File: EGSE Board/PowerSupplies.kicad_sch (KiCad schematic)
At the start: 30 parts, among them U1 VOR2121A8, U2 VOR2121A8, U3 INA238AQDGSRQ1, U4 INA238AQDGSRQ1, U5 INA238AQDGSRQ1, U7 ISO1540, U9 LD1117S33TR_SOT223

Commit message: Change to heater power
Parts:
- removed C10: 100nF, symbol Device:C_Small
- removed C7, C9: 10nF, symbol Device:C_Small
- removed U3, U5: INA238AQDGSRQ1, Package_SO:VSSOP-10_3x3mm_P0.5mm, symbol Power_Management:INA238AQDGSRQ1
- added C3, C5: 100nF, symbol Device:C_Small
- added R1: 0.1R, symbol Device:R
- added U14: INA3221, Package_DFN_QFN:Texas_RGV_S-PVQFN-N16_EP2.1x2.1mm, symbol Power_Management:INA3221
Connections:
- net +3V3: now also C5.1, U14.4 (VS)
- net DETEC_+12VA: now also U14.11 (IN-1)
- net DETEC_+3v3: now also U14.14 (IN-2)
- net GND: now also C3.2, C5.2, U14.3 (GND)
- net SCL: now also U14.6 (SCL)
- net SDA: now also U14.7 (SDA)
- net at R1.1, U1.7 (S1'): now also U14.12 (IN+1)
- net at R5.1, U2.8 (S1): now also U14.15 (IN+2)
- new net: R1.1, U14.2 (IN+3)
- new net DETEC_HTR: C3.1, R1.2, U14.1 (IN-3)
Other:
- note added: "I2C current monitors for +12 and +3v3 and heater supplies"
- note removed: "I2C current monitors for +12 and +3v3 supplies"
- moved on the sheet: C5, C6, R1, R5

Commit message: Friday updates. PCB first draft
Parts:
- C1, C2, C6: footprint (none) -> Capacitor_Tantalum_SMD:CP_EIA-7343-31_Kemet-D_Pad2.25x2.55mm_HandSolder
- C10, C3, C4, C5, C8: footprint (none) -> Capacitor_SMD:C_0402_1005Metric
- R1, R5: footprint (none) -> Resistor_THT:R_Axial_DIN0207_L6.3mm_D2.5mm_P7.62mm_Horizontal
- R1, R2: value 1R -> 0.1R; footprint (none) -> Resistor_THT:R_Axial_DIN0207_L6.3mm_D2.5mm_P7.62mm_Horizontal
- R13, R14, R3, R4, R6: footprint (none) -> Resistor_SMD:R_0612_1632Metric
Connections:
- net +3V3: now also U1.6 (S2); no longer U2.7 (S1')
- net -12V_Unswitched: now also U2.6 (S2); no longer U1.5 (S2'), U4.2 (A0)
- net DETEC_+12VA: now also U14.1 (IN-3); no longer U14.11 (IN-1)
- net DETEC_+3v3: now also U14.11 (IN-1); no longer U14.14 (IN-2)
- net DETEC_HTR: now also U14.14 (IN-2); no longer U14.1 (IN-3)
- net GND: now also U14.5 (A0), U2.4; no longer U2.2
- net at C10.2, C3.1, R13.1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: now also U4.2 (A0)
- net at C8.1, R2.1, U4.10 (IN+): now also U2.5 (S2'); no longer U1.6 (S2)
- net at R6.2: now also U1.3; no longer U2.1
- net at U14.2 (IN+3): now also R1.1, U1.7 (S1'); no longer R1.1
- net at U2.3: now also R4.2
- net +12_Unswitched: no longer names the net of C5.1, PS1.6 (+Vout), U1.8 (S1)
- new net: R5.1, U1.5 (S2'), U14.12 (IN+1)
- new net +12V_HTR: R1.1, U14.15 (IN+2)
- now unconnected: U2.8 (S1)
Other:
- note added: "A0,A1=Vs, address=0x45"
- note added: "A0=GND Address=0x40"
- moved on the sheet: C3, C5, C6, R1, R3, R4, R5, R6, U1, U14, U2

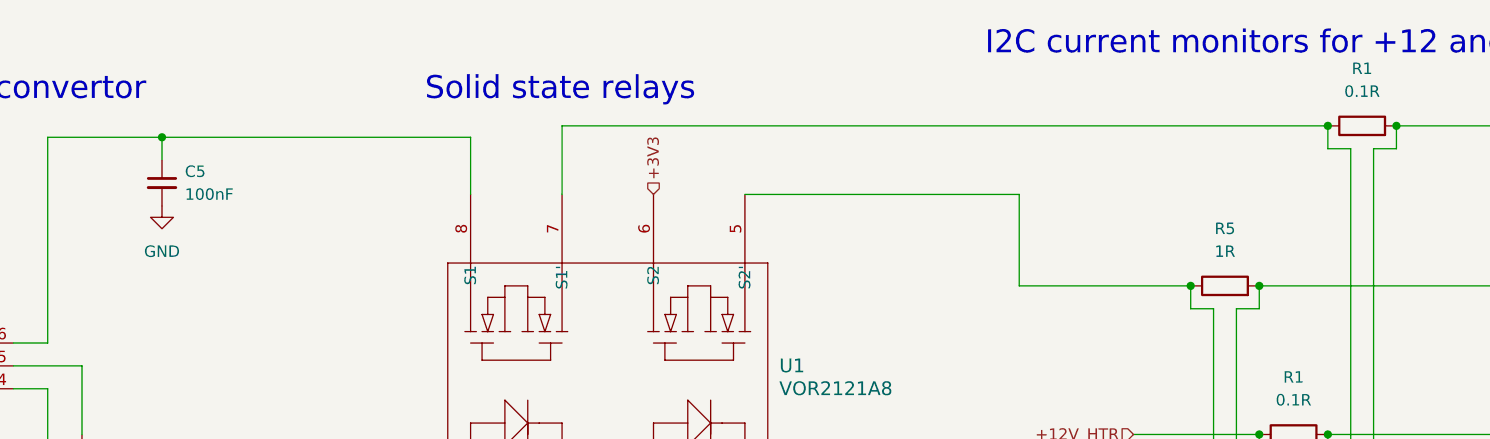
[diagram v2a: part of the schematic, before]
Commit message: Regular update
Created Gerber files for production
Changed names in arduino code to reflect signal names used by MSSL and on EGSE board
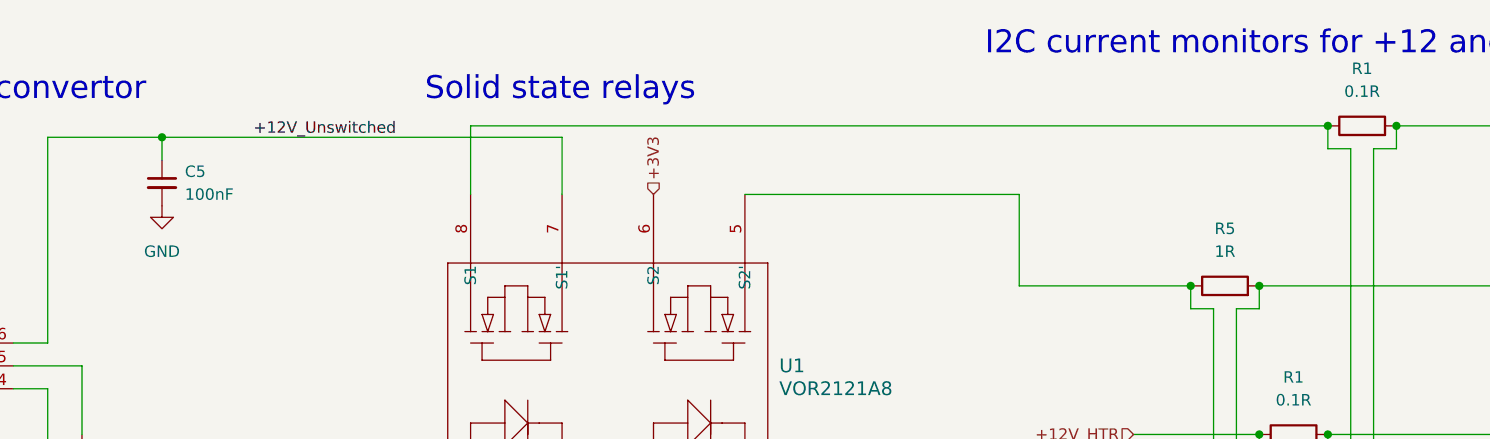
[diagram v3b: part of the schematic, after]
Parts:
- R13, R14, R3, R4, R6: footprint Resistor_SMD:R_0612_1632Metric -> Resistor_SMD:R_0805_2012Metric
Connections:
- net at R1.1, U14.2 (IN+3): now also U1.8 (S1); no longer U1.7 (S1')
- net +12V_Unswitched: now reaches C5.1, PS1.6 (+Vout)
- net +12V_Unswitched: now also U1.7 (S1'); no longer U1.8 (S1)
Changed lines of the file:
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@@
     (stroke (width 0) (type default))
   )
-  (wire (pts (xy 63.5 26.67) (xy 97.79 26.67))
+  (wire (pts (xy 63.5 26.67) (xy 107.95 26.67))
     (stroke (width 0) (type default))
   )
@@
     (stroke (width 0) (type default))
   )
-  (wire (pts (xy 107.95 25.4) (xy 193.04 25.4))
+  (wire (pts (xy 97.79 25.4) (xy 193.04 25.4))
     (stroke (width 0) (type default))
   )
@@
     (stroke (width 0) (type default))
   )
+  (wire (pts (xy 97.79 25.4) (xy 97.79 33.02))
+    (stroke (width 0) (type default))
+  )
   (wire (pts (xy 240.03 43.18) (xy 252.73 43.18))
     (stroke (width 0) (type default))
@@
     (stroke (width 0) (type default))
   )
-  (wire (pts (xy 97.79 26.67) (xy 97.79 33.02))
-    (stroke (width 0) (type default))
-  )
   (wire (pts (xy 114.3 130.81) (xy 109.22 130.81))
     (stroke (width 0) (type default))
@@
     (stroke (width 0) (type default))
   )
-  (wire (pts (xy 107.95 33.02) (xy 107.95 25.4))
-    (stroke (width 0) (type default))
-  )
   (wire (pts (xy 114.3 132.08) (xy 114.3 130.81))
     (stroke (width 0) (type default))
@@
   )
   (wire (pts (xy 182.88 45.72) (xy 182.88 66.04))
+    (stroke (width 0) (type default))
+  )
+  (wire (pts (xy 107.95 26.67) (xy 107.95 33.02))
     (stroke (width 0) (type default))
   )
@@
   (text "Regulator\ngives 3v3 reference \nabove -12V line\n" (at 29.21 176.53 0)
     (effects (font (size 2.54 2.54)) (justify left bottom))
+  )
+  (label "+12V_Unswitched" (at 73.66 26.67 0) (fields_autoplaced)
+    (effects (font (size 1.27 1.27)) (justify left bottom))
   )
   (label "SCL" (at 81.28 146.05 0) (fields_autoplaced)
@@
       (effects (font (size 1.27 1.27)))
     )
-    (property "Footprint" "Resistor_SMD:R_0612_1632Metric" (at 80.01 81.788 90)
+    (property "Footprint" "Resistor_SMD:R_0805_2012Metric" (at 80.01 81.788 90)
       (effects (font (size 1.27 1.27)) hide)
     )
@@
       (effects (font (size 1.27 1.27)))
     )
-    (property "Footprint" "Resistor_SMD:R_0612_1632Metric" (at 87.63 130.048 90)
+    (property "Footprint" "Resistor_SMD:R_0805_2012Metric" (at 87.63 130.048 90)
       (effects (font (size 1.27 1.27)) hide)
     )
@@
       (effects (font (size 1.27 1.27)) (justify left))
     )
-    (property "Footprint" "Resistor_SMD:R_0612_1632Metric" (at 112.522 135.89 90)
+    (property "Footprint" "Resistor_SMD:R_0805_2012Metric" (at 112.522 135.89 90)
       (effects (font (size 1.27 1.27)) hide)
     )
@@
       (effects (font (size 1.27 1.27)))
     )
-    (property "Footprint" "Resistor_SMD:R_0612_1632Metric" (at 87.63 75.438 90)
+    (property "Footprint" "Resistor_SMD:R_0805_2012Metric" (at 87.63 75.438 90)
       (effects (font (size 1.27 1.27)) hide)
     )
@@
       (effects (font (size 1.27 1.27)) (justify left))
     )
-    (property "Footprint" "Resistor_SMD:R_0612_1632Metric" (at 120.142 135.89 90)
-      (effects (font (size 1.27 1.27)) hide)
-    )
+    (property "Footprint" "Resistor_SMD:R_0805_2012Metric" (at 120.142 135.89 90)
+      (effects (font (size 1.27 1.27)) hide)
+    )
